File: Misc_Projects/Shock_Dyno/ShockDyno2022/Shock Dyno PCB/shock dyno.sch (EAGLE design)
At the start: 13 parts, among them J1 1985205

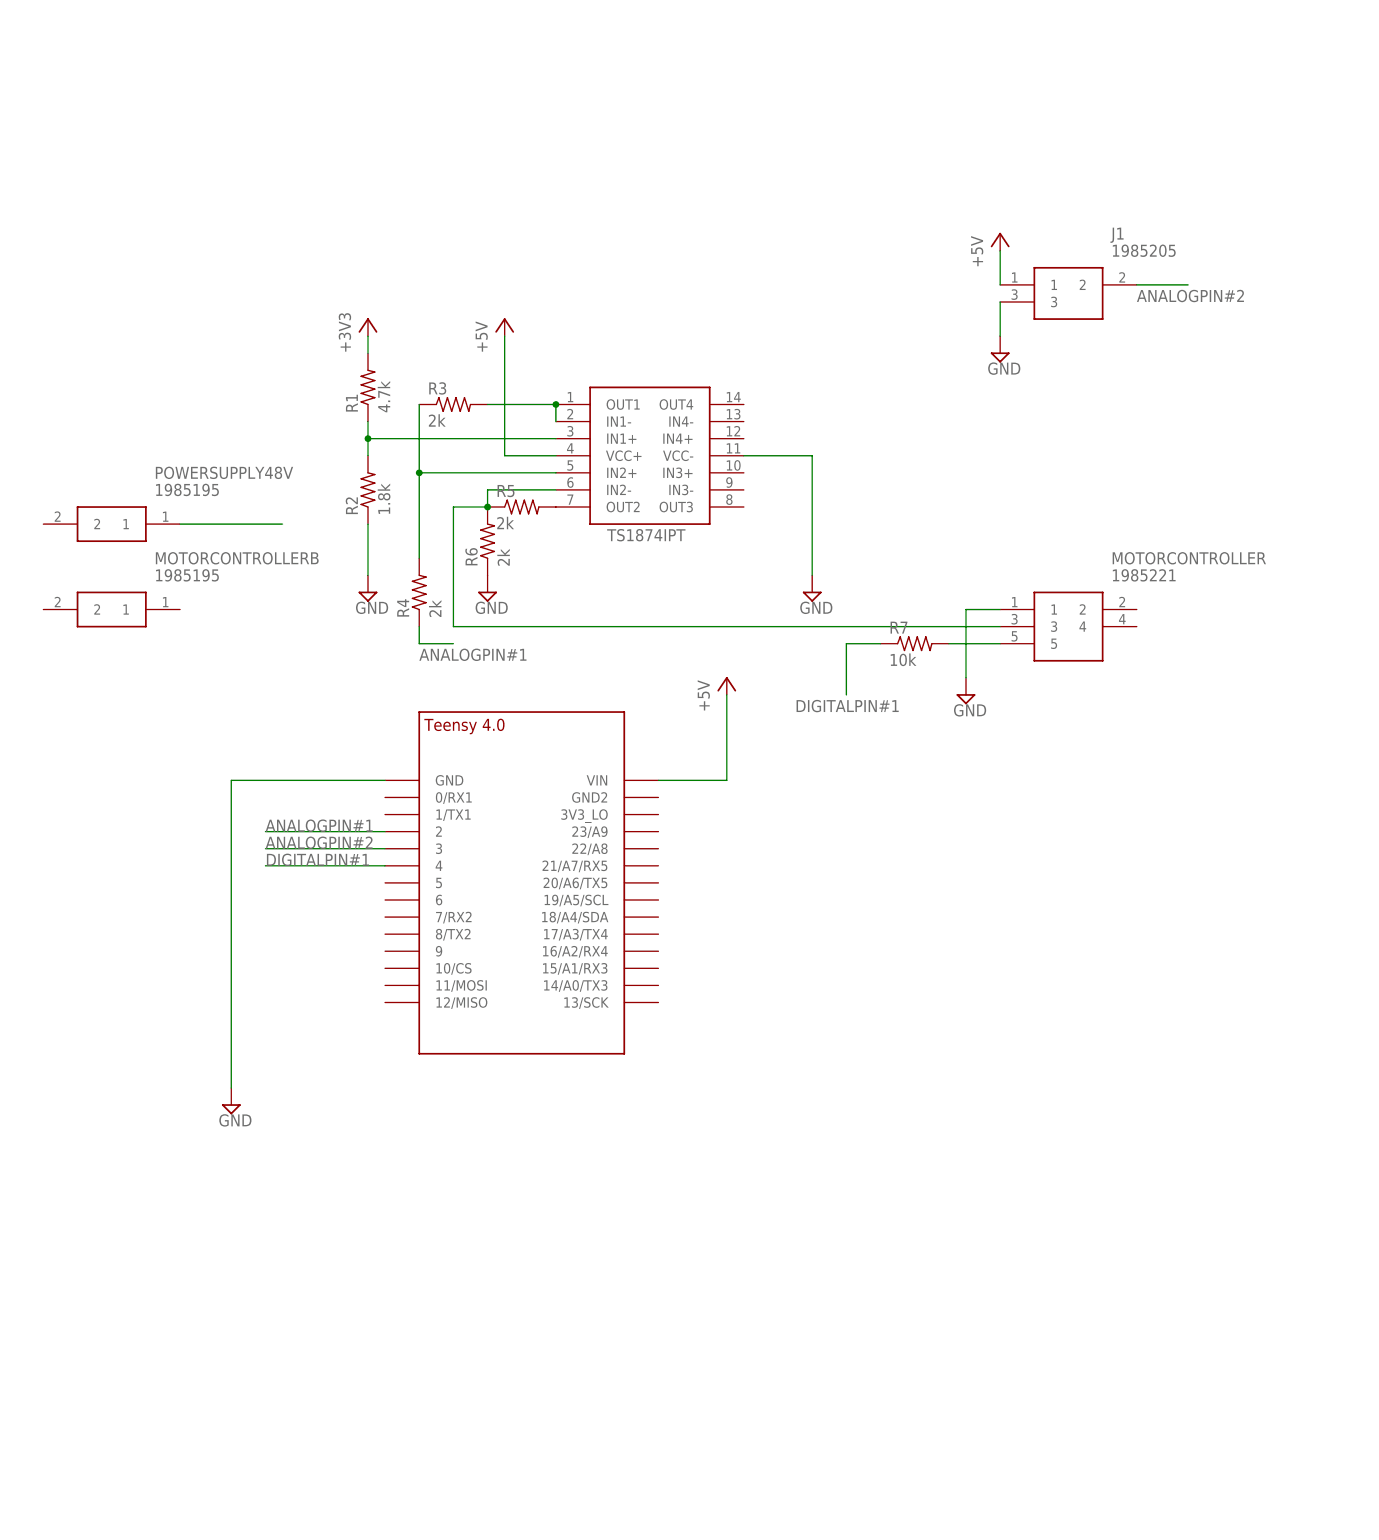
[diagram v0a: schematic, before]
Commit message: added MOSFET circuit and power relay for shock dyno pcb
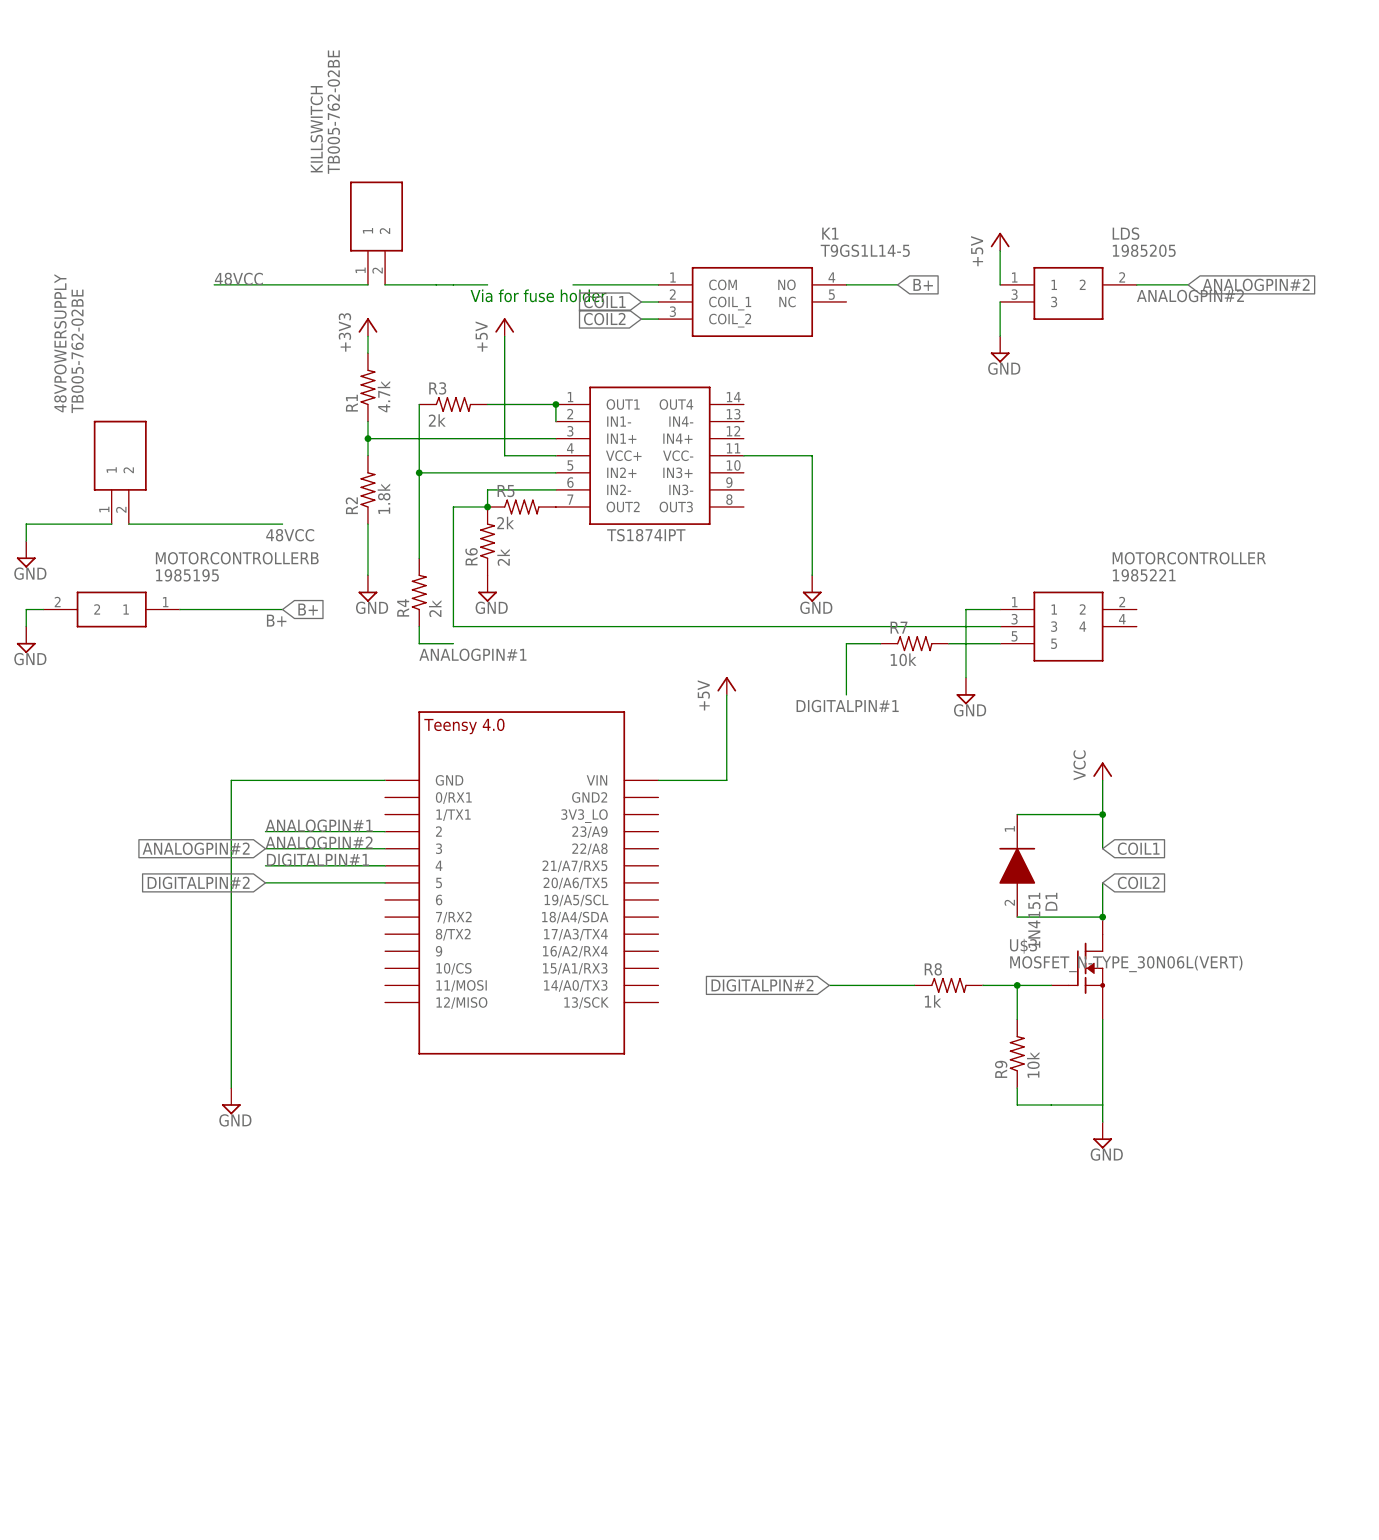
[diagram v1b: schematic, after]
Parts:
- removed POWERSUPPLY48V: 1985195, 1985195:1985195
- added 48VPOWERSUPPLY, KILLSWITCH: TB005-762-02BE, GTOR - Connectors:TB005-762-02BE
- added D1: 1N4151, GTOR - Passive Components:1N4151
- added K1: T9GS1L14-5, GTOR - Active Components:T9GS1L14-5
- added R8: 1k, GTOR - Passive Components:RES_SMDR0603
- added R9: 10k, GTOR - Passive Components:RES_SMDR0603
- added U$3: MOSFET_N-TYPE_30N06L(VERT), GTOR - Active Components:MOSFET_N-TYPE_30N06L(VERT)
- renumbered J1 to LDS
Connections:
- new net 48VCC: 48VPOWERSUPPLY.2, KILLSWITCH.1
- new net B+: K1.NO, MOTORCONTROLLERB.1
- new net COIL1: D1.K, K1.COIL_1
- new net COIL2: D1.A, K1.COIL_2, U$3.D
- new net DIGITALPIN#2: R8.1, U$2.5
- new net N$11: R8.2, R9.2, U$3.G
- new net N$8: K1.COM
- net GND: now also 48VPOWERSUPPLY.1, MOTORCONTROLLERB.2, R9.1, U$3.S
- net N$6: now also KILLSWITCH.2; no longer POWERSUPPLY48V.1
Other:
- note added: "Via for fuse holder"

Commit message: completed shock dyno PCB schematic
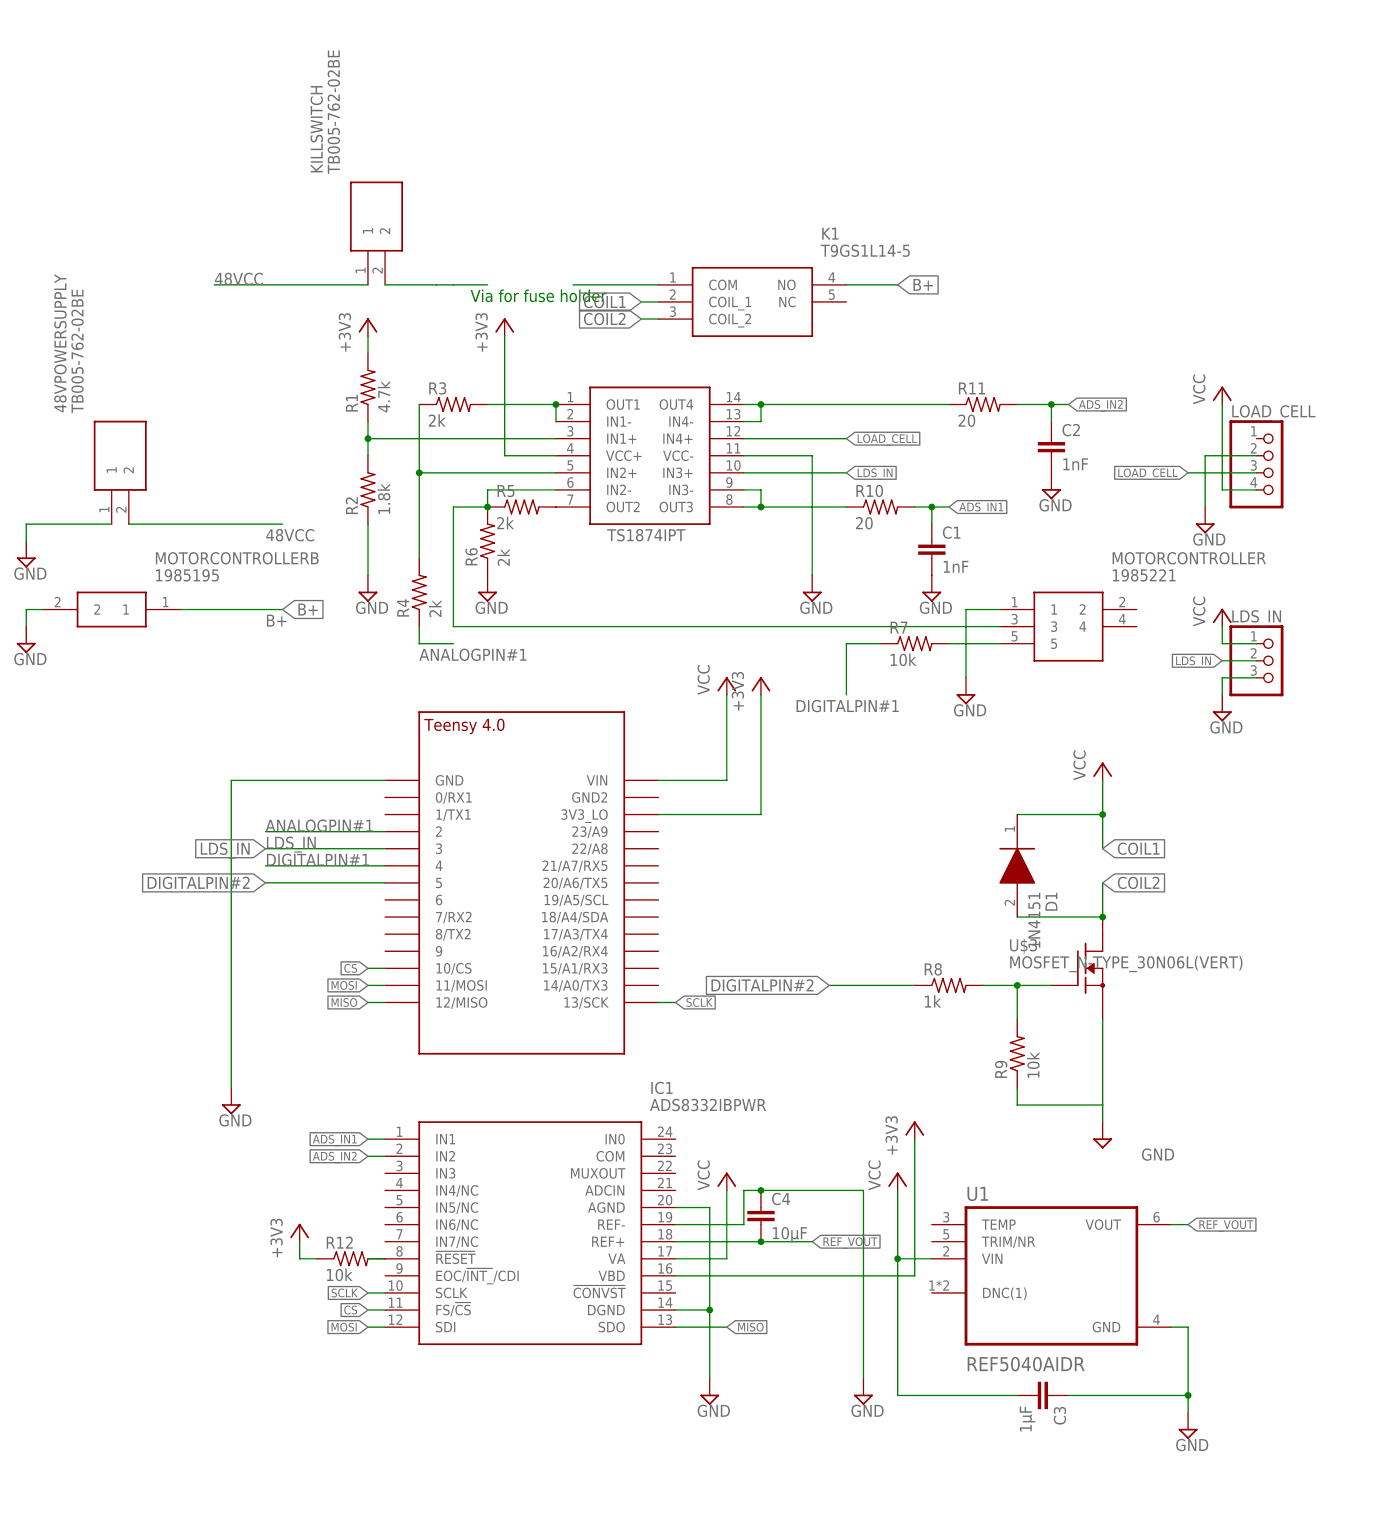
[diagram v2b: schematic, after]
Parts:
- removed LDS: 1985205, 1985205:1985205
- added C1, C2: 1nF, GTOR - Passive Components:CAP_SMDC0603
- added C3: 1μF, GTOR - Passive Components:CAP_SMDC0603
- added C4: 10μF, GTOR - Passive Components:CAP_SMDC0603
- added IC1: ADS8332IBPWR, GTOR - Active Components:ADS8332IBPWR
- added LDS_IN: (no value), GTOR - Connectors:PINHD-1X3
- added LOAD_CELL: (no value), GTOR - Connectors:PINHD-1X4
- added R10, R11: 20, GTOR - Passive Components:RES_SMDR0603
- added R12: 10k, GTOR - Passive Components:RES_SMDR0603
- added U1: REF5040AIDR, GTOR - Active Components:REF5040AIDR
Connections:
- removed net +5V: LDS.1, U$1.VCC+, U$2.VIN
- removed net ANALOGPIN#2: LDS.2, U$2.3
- new net ADS_IN1: C1.1, IC1.IN1, R10.2
- new net ADS_IN2: C2.1, IC1.IN2, R11.2
- new net CS: IC1.FS/!CS, U$2.10/CS
- new net LDS_IN: LDS_IN.2, U$1.IN3+, U$2.3
- new net LOAD_CELL: LOAD_CELL.3, U$1.IN4+
- new net MISO: IC1.SDO, U$2.12/MISO
- new net MOSI: IC1.SDI, U$2.11/MOSI
- new net N$10: R10.1, U$1.IN3-, U$1.OUT3
- new net N$12: IC1.!RESET, R12.2
- new net N$9: R11.1, U$1.IN4-, U$1.OUT4
- new net REF_VOUT: C4.2, IC1.REF+, U1.VOUT
- new net SCLK: IC1.SCLK, U$2.13/SCK
- new net VCC: C3.2, IC1.VA, LDS_IN.1, LOAD_CELL.4, U$2.VIN, U1.VIN
- net +3V3: now also IC1.VBD, R12.1, U$1.VCC+, U$2.3V3_LO
- net GND: now also C1.2, C2.2, C3.1, C4.1, IC1.AGND, IC1.DGND, IC1.REF-, LDS_IN.3, LOAD_CELL.2, U1.GND; no longer LDS.3
